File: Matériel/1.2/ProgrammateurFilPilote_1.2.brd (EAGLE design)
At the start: 85.5 x 66.8 mm, 78 parts, among them IC2 MCP23017, J2 GROVE-I2C, P1 PADSMALL, P2 PADSMALL, SW1 HLS8L-DC5V-S-C, T1 2N2222

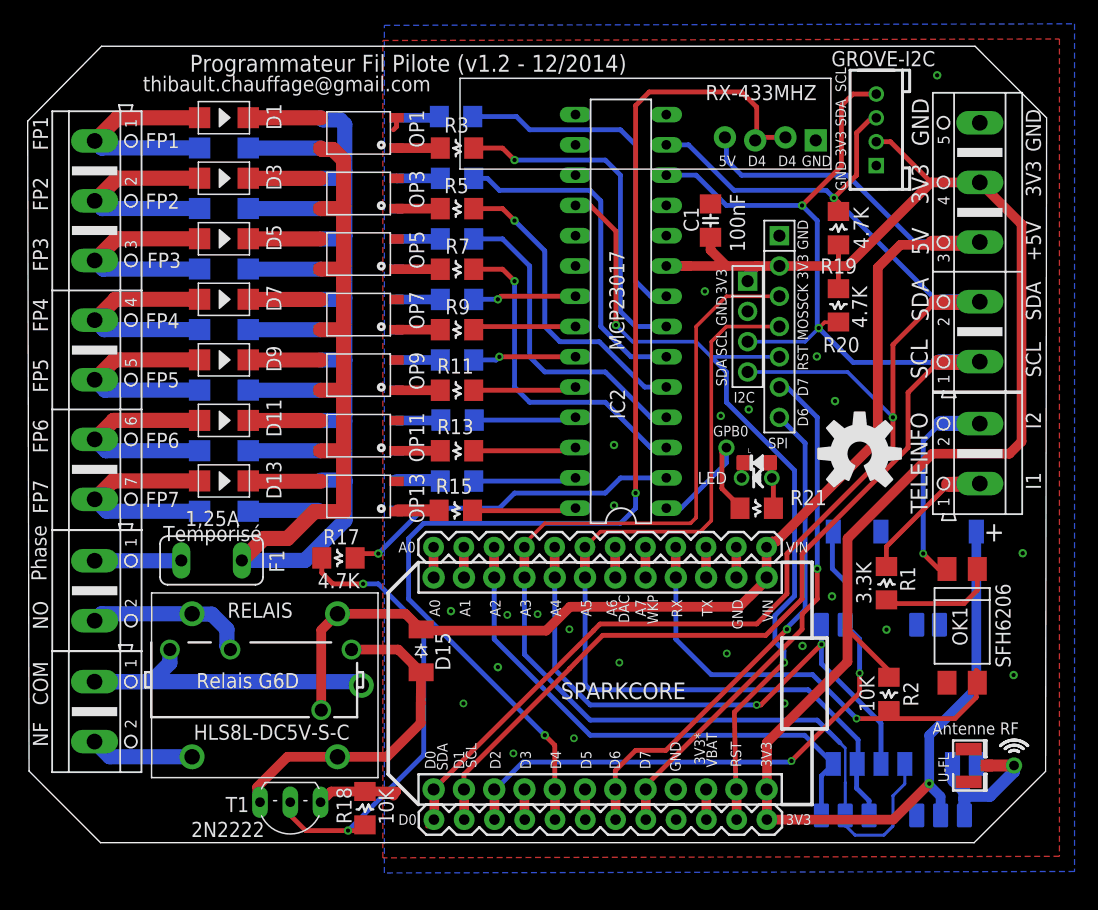
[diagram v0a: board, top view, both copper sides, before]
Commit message: Revert "Màj v1.2"
This reverts commit 1069f649c9f2bcb6078a36c473411e82ae330c49.
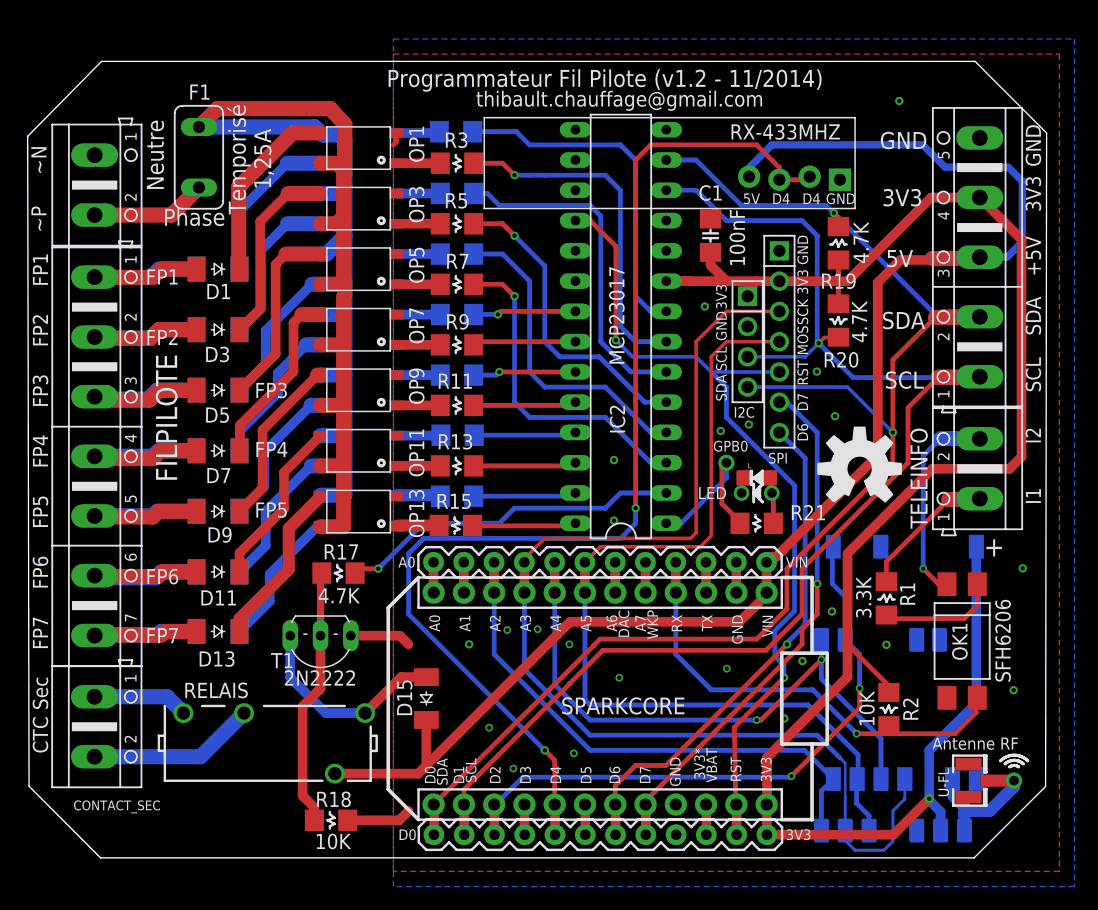
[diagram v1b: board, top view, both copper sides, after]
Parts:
- removed J2: GROVE-I2C, seeed-opl-Connector:4P-2.0
- removed RL: (no value), con-ptr500:AK500/2
- removed SW1: HLS8L-DC5V-S-C, seeed-opl-Connector:5P-L19.0XW15.0XH15.0MM
- added CONTACT_SEC: (no value), con-ptr500:AK500/2
- D1, D10, D11, D12, D13, D14, D2, D3, D4, D5, D6, D7, D8, D9: value SL1J -> CGRM4001-G; device seeed-opl-Discrete:DO-214AC -> diode:SOD-123_MINI-SMA
- moved 230V 34.0 mm to (5.41, 55.0)
- moved F1 33.8 mm to (14.2, 57.4), turned to 90 degrees
- moved T1 14.2 mm to (24.4, 16.0)
- moved D1 12.7 mm to (15.8, 48.0), turned to 180 degrees
- moved D9 12.7 mm to (15.8, 27.7), turned to 180 degrees
- moved D11 12.7 mm to (15.8, 22.6), turned to 180 degrees
- moved D3 12.7 mm to (15.8, 42.9), turned to 180 degrees
- moved D5 12.7 mm to (15.8, 37.8), turned to 180 degrees
- moved D7 12.7 mm to (15.8, 32.8), turned to 180 degrees
- moved D13 12.6 mm to (15.8, 17.6), turned to 180 degrees
- moved FILPILOTE 11.4 mm to (5.41, 32.3)
- moved D12 10.2 mm to (15.8, 22.6), turned to 180 degrees
- moved D2 10.2 mm to (15.8, 48.0), turned to 180 degrees
- moved D4 10.2 mm to (15.8, 42.9), turned to 180 degrees
- moved D6 10.2 mm to (15.8, 37.8), turned to 180 degrees
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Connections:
- removed net COM: RELAIS.7, RL.1, SW1.1
- removed net N$16: 230V.1, F1.1
- removed net NF: RL.2, SW1.5
- removed net NO: 230V.2, RELAIS.5, SW1.4
- new net N$17: 230V.2, F1.1
- new net N$18: CONTACT_SEC.2, RELAIS.5
- new net N$20: CONTACT_SEC.1, RELAIS.7
- new net NEUTRE: 230V.1
- net +3V3: no longer J2.2
- net +5V: no longer SW1.2
- net FP1: now also D1.A, D2.C; no longer D1.1, D2.2
- net FP2: now also D3.A, D4.C; no longer D3.1, D4.2
- net FP3: now also D5.A, D6.C; no longer D5.1, D6.2
- net FP4: now also D7.A, D8.C; no longer D7.1, D8.2
- net FP5: now also D10.C, D9.A; no longer D10.2, D9.1
- net FP6: now also D11.A, D12.C; no longer D11.1, D12.2
- net FP7: now also D13.A, D14.C; no longer D13.1, D14.1
- net GND: no longer J2.1
- net N$1: now also D1.C; no longer D1.2
- net N$15: no longer SW1.3
- net N$2: now also D2.A; no longer D2.1
- net N$22: now also D3.C; no longer D3.2
- net N$24: now also D5.C; no longer D5.2
- net N$25: now also D4.A; no longer D4.1
- net N$26: now also D7.C; no longer D7.2
- net N$29: now also D6.A; no longer D6.1
- net N$31: now also D8.A; no longer D8.1
- net N$42: now also D9.C; no longer D9.2
- net N$49: now also D10.A; no longer D10.1
- net N$51: now also D12.A; no longer D12.1
- net S$1: now also D11.C; no longer D11.2
- net S$11: now also D14.A; no longer D14.2
- net S$3: now also D13.C; no longer D13.2
- net SCL: no longer J2.4
- net SDA: no longer J2.3
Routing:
- net COM: track 30.3 -> 0.00 mm
- net N$21: track 39.5 -> 21.8 mm, vias 2 -> 0
- net N$18: track 0.00 -> 14.1 mm
- net NO: track 13.7 -> 0.00 mm
- net SCL: track 130.2 -> 117.2 mm, vias 2 -> 1
- net PHASE: track 111.3 -> 123.0 mm
- net N$15: track 28.2 -> 17.4 mm
- net N$24: track 6.10 -> 16.0 mm
- net N$22: track 6.10 -> 15.9 mm
- net N$17: track 0.00 -> 9.71 mm
- net N$1: track 6.10 -> 15.7 mm
- net N$26: track 6.10 -> 15.2 mm
- net NF: track 8.71 -> 0.00 mm
- net SDA: track 131.8 -> 123.3 mm
- net N$42: track 6.10 -> 14.4 mm
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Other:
- board text added: "CTC Sec"
- board text added: "D'"
- board text added: "Neutre"
- board text added: "Programmateur Fil Pilote (v1.2 - 11/2014)"
- board text added: "Temporisé 1,25A"
- board text added: "~N"
- board text added: "~P"
- board text removed: "1,25A"
- board text removed: "COM"
- board text removed: "NF"
- board text removed: "NO"
- board text removed: "Programmateur Fil Pilote (v1.2 - 12/2014)"
- board text removed: "Temporisé"
